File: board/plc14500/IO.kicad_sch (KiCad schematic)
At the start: 71 parts, among them U1 74HC14, U2 4051, U3 74HC14, U5 4099, U6 Arduino Nano

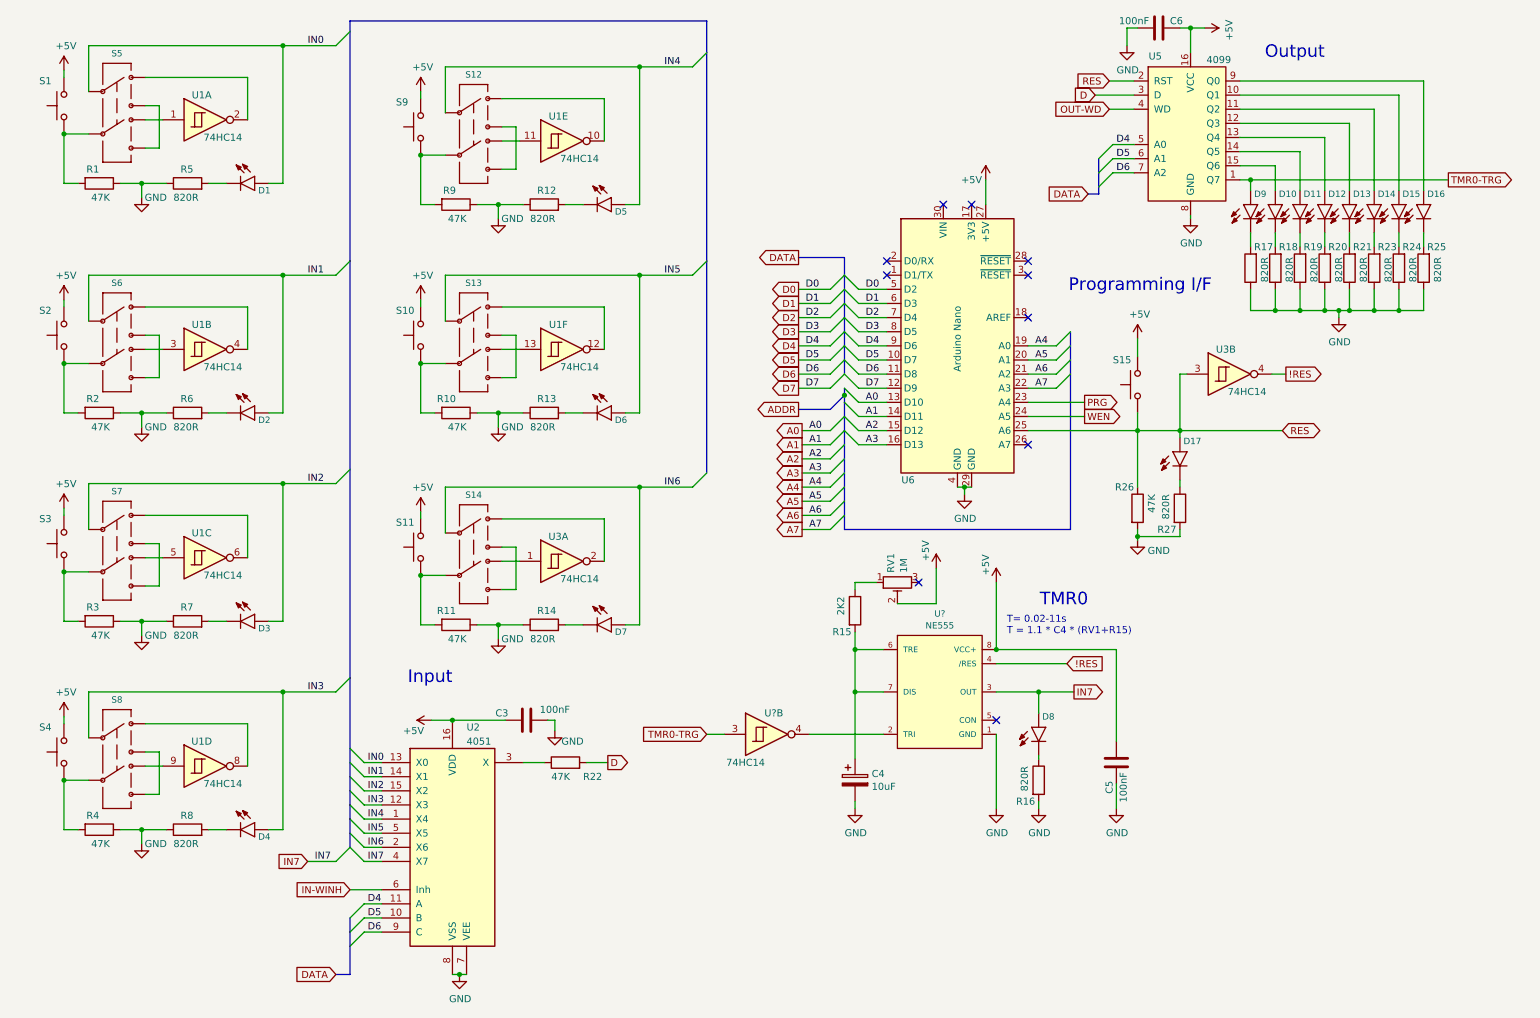
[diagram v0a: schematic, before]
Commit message: Rearrange LEDs
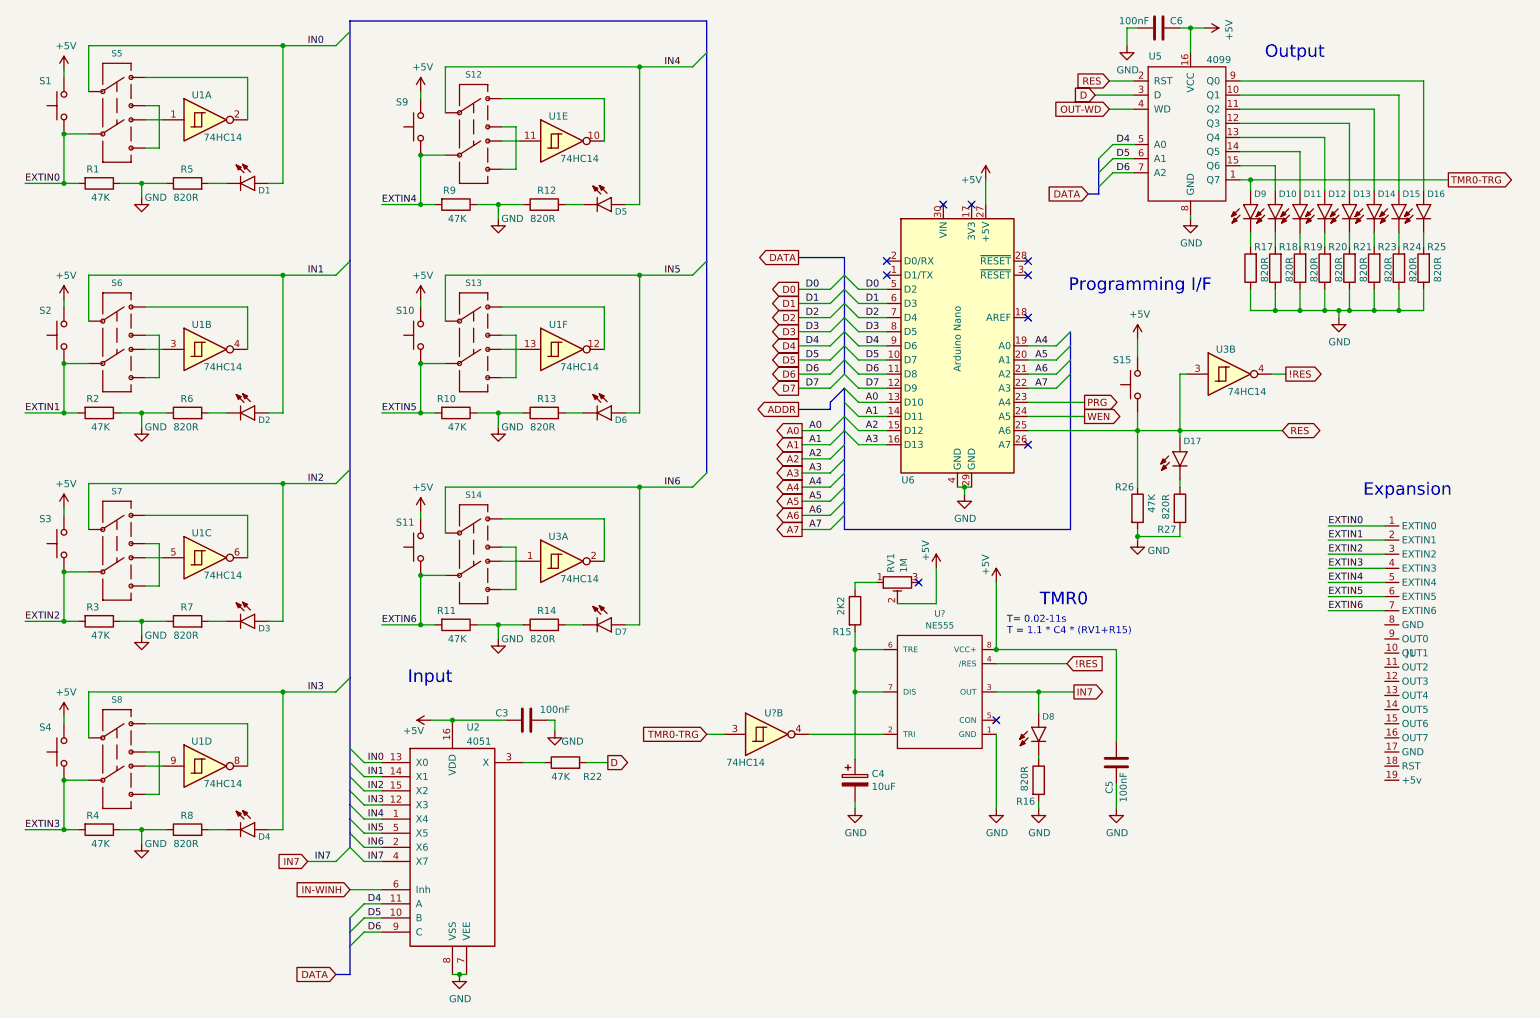
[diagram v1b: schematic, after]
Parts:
- added J1: ~, symbol plc14500:PLC14500-Expansion
- U2: symbol 4xxx:4051 -> plc14500:4051
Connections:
- net EXTIN0: now reaches R1.2, S1.1, S5.6
- net EXTIN0: now also J1.1 (EXTIN0)
- net EXTIN1: now reaches R2.2, S2.1, S6.6
- net EXTIN1: now also J1.2 (EXTIN1)
- net EXTIN2: now reaches R3.2, S3.1, S7.6
- net EXTIN2: now also J1.3 (EXTIN2)
- net EXTIN3: now reaches R4.2, S4.1, S8.6
- net EXTIN3: now also J1.4 (EXTIN3)
- net EXTIN4: now reaches R9.2, S12.6, S9.1
- net EXTIN4: now also J1.5 (EXTIN4)
- net EXTIN5: now reaches R10.2, S10.1, S13.6
- net EXTIN5: now also J1.6 (EXTIN5)
- net EXTIN6: now reaches R11.2, S11.1, S14.6
- net EXTIN6: now also J1.7 (EXTIN6)
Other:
- note added: "Expansion"

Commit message: REV.D Schema updates
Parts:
- removed D17: LED 3MM Red, plc14500:LED_3MM, symbol plc14500-rescue:LED5MM-SparkFun-LED
- removed R26: 47K, Resistor_THT:R_Axial_DIN0204_L3.6mm_D1.6mm_P7.62mm_Horizontal, symbol Device:R
- removed R27: 820R, Resistor_THT:R_Axial_DIN0204_L3.6mm_D1.6mm_P7.62mm_Horizontal, symbol Device:R
- removed S15: Push Button, plc14500:SW_Tactile_THT, symbol Switch:SW_Push
- removed unit 2 of U3
- removed U6: Arduino Nano, Module:Arduino_Nano, symbol MCU_Module:Arduino_Nano_v2.x
- added C1, C2: 100nF, Capacitor_THT:C_Rect_L7.2mm_W2.5mm_P5.00mm_FKS2_FKP2_MKS2_MKP2, symbol Device:C
- added unit 7 of U1
- added unit 7 of U3
- S12, S13, S14, S5, S6, S7, S8: symbol plc14500-rescue:SWITCH-DPDT-PTH-GPI-152-3013-SparkFun-Switches -> plc14500:SWITCH-DPDT
- U1, U3, U?: symbol 74xx:74HC14 -> plc14500:74HC14
- U?: symbol plc14500-rescue:555D-SparkFun-IC-Special-Function -> plc14500:555
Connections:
- net +5V: now also C3.1, J1.18 (+5v), C1.2, C2.2, U1.14 (VCC), U3.14 (VCC); no longer C3.2
- net GND: now also C3.2, J1.8 (GND), C1.1, C2.1, U1.7 (GND), U3.7 (GND); no longer C3.1
- net RES: no longer U5.2 (RST)
- net at S5.1: now also S5.5, S5.7, U1.1; no longer U1.2
- net at S5.3: now also U1.2; no longer S5.7
- net at S6.1: now also S6.5, S6.7, U1.3; no longer U1.4
- net at S6.3: now also U1.4; no longer S6.7
- net at S7.1: now also S7.5, S7.7, U1.5; no longer U1.6
- net at S7.3: now also U1.6; no longer S7.7
- net at S8.1: now also S8.5, S8.7, U1.9; no longer U1.8
- net at S8.3: now also U1.8; no longer S8.7
- net at S12.1: now also S12.5; no longer U1.10
- net at S12.3: now also U1.10; no longer S12.7
- net at U1.11: now also S12.7; no longer S12.5
- net at S13.1: now also S13.5; no longer U1.12
- net at S13.3: now also U1.12; no longer S13.7
- net at U1.13: now also S13.7; no longer S13.5
- net at S14.1: now also S14.5; no longer U3.2
- net at S14.3: now also U3.2; no longer S14.7
- net at U3.1: now also S14.7; no longer S14.5
- net OUT1: now reaches J1.10 (OUT1)
- net OUT2: now reaches J1.11 (OUT2)
- net OUT3: now reaches J1.12 (OUT3)
- net OUT4: now reaches J1.13 (OUT4)
- net OUT5: now reaches J1.14 (OUT5)
- net OUT6: now reaches J1.15 (OUT6)
- net OUT7: now reaches J1.16 (OUT7)
- net RST: now reaches J1.17 (RST)
- net RST: now also U5.2 (RST)
- net OUT0: now reaches J1.9 (OUT0)
- net IN-WINH renamed IN-INH
- no-connect marks 10 -> 2
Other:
- note added: "Input Selector"
- note added: "Output Latch"
- note removed: "Input"
- note removed: "Output"
- note removed: "Programming I/F"
- moved on the sheet: C3, C4, C5, C6, D1, D10, D11, D12, D13, D14, D15, D16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

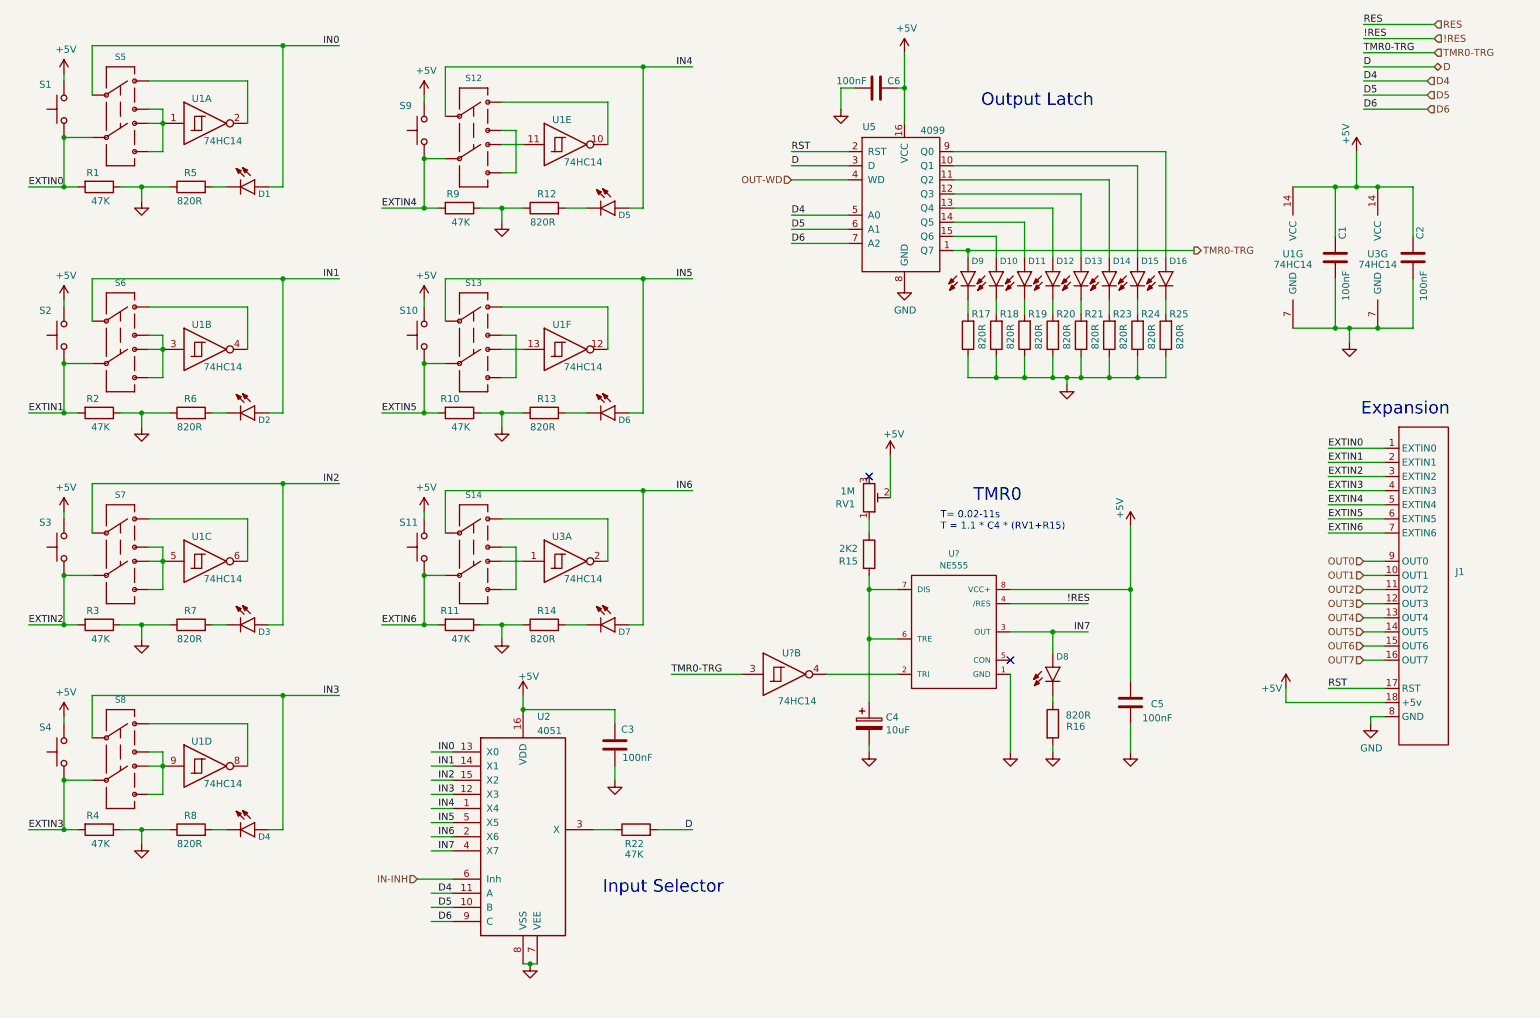
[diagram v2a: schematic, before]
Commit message: Address ERC errors
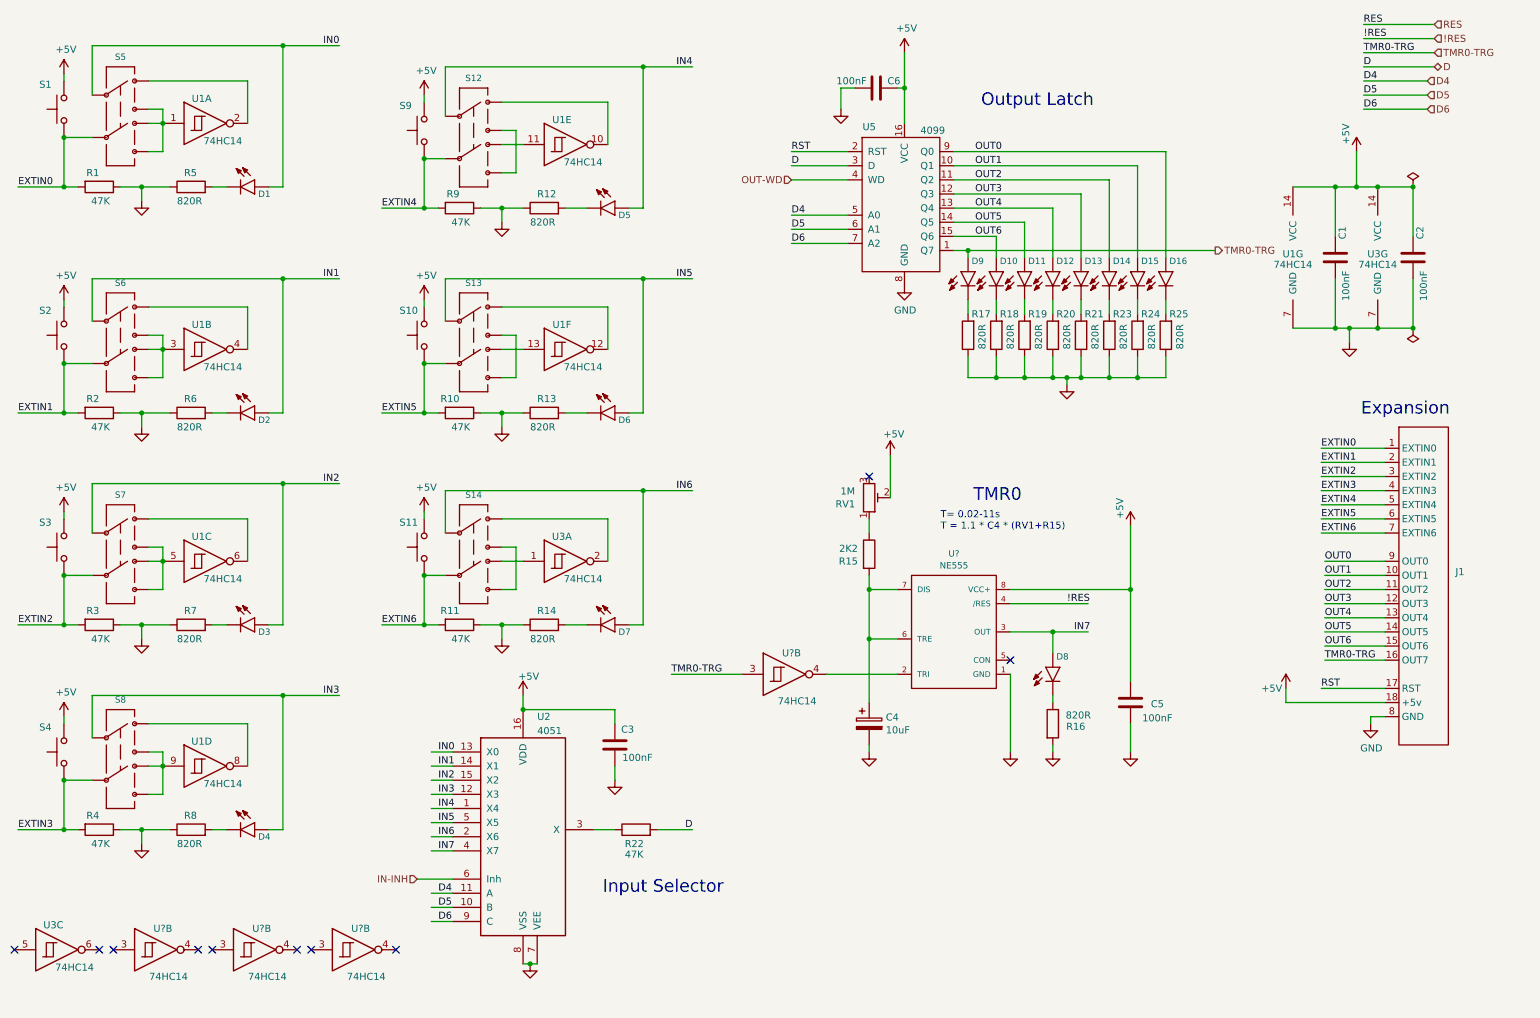
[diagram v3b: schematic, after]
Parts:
- added unit 3 of U3
- added U? (x3): 74HC14, Package_DIP:DIP-14_W7.62mm_LongPads, symbol plc14500:74HC14
- C4: symbol plc14500-rescue:CP-Device -> plc14500:CP-Device
- D1, D10, D11, D12, D13, D14, D15, D16, D2, D3, D4, D5, D6, D7, D8, D9: footprint plc14500:LED_3MM -> LED_5MM; symbol plc14500-rescue:LED5MM-SparkFun-LED -> plc14500:LED
- RV1: symbol plc14500-rescue:R_POT_TRIM-Device -> plc14500:Trimmer
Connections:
- net OUT7 is gone; now on net TMR0-TRG: J1.16 (OUT7)
- net OUT0: now also D16.A, U5.9 (Q0)
- net OUT1: now also D15.A, U5.10 (Q1)
- net OUT2: now also D14.A, U5.11 (Q2)
- net OUT3: now also D13.A, U5.12 (Q3)
- net OUT4: now also D12.A, U5.13 (Q4)
- net OUT5: now also D11.A, U5.14 (Q5)
- net OUT6: now also D10.A, U5.15 (Q6)
- no-connect marks 2 -> 10
